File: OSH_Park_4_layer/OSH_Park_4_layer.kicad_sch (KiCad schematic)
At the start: 2 parts

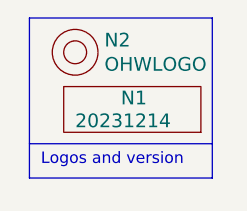
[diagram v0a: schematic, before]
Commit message: updated to kicad V8
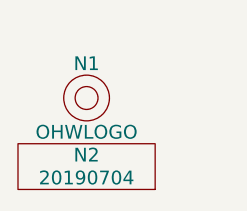
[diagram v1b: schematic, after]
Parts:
- removed N1: 20231214, SquantorLabels:Label_Generic, symbol SquantorLabels:VYYYYMMDD
- removed N2: OHWLOGO, Symbol:OSHW-Symbol_6.7x6mm_SilkScreen, symbol SquantorLabels:OHWLOGO
- added N1: OHWLOGO, Symbols:OSHW-Symbol_6.7x6mm_SilkScreen, symbol SquantorLabels:OHWLOGO
- added N2: 20190704, SquantorLabels:Label_version, symbol SquantorLabels:VYYYYMMDD
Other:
- note removed: "Logos and version"
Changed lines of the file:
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@@
 	(generator_version "8.0")
 	(paper "A4")
-	(polyline
-		(pts
-			(xy 15.24 177.8) (xy 15.24 195.58)
-		)
-		(stroke
-			(width 0)
-			(type default)
-		)
-	)
-	(polyline
-		(pts
-			(xy 35.56 177.8) (xy 15.24 177.8)
-		)
-		(stroke
-			(width 0)
-			(type default)
-		)
-	)
-	(polyline
-		(pts
-			(xy 35.56 195.58) (xy 35.56 177.8)
-		)
-		(stroke
-			(width 0)
-			(type default)
-		)
-	)
-	(polyline
-		(pts
-			(xy 15.24 195.58) (xy 35.56 195.58)
-		)
-		(stroke
-			(width 0)
-			(type default)
-		)
-	)
-	(polyline
-		(pts
-			(xy 15.24 191.77) (xy 35.56 191.77)
-		)
-		(stroke
-			(width 0)
-			(type default)
-		)
-	)
-	(text "Logos and version"
-		(exclude_from_sim no)
-		(at 16.51 194.31 0)
-		(effects
-			(font
-				(size 1.27 1.27)
-			)
-			(justify left bottom)
-		)
-	)
 	(symbol
 		(lib_id "SquantorLabels:VYYYYMMDD")
-		(at 26.67 189.23 0)
+		(at 21.59 195.58 0)
 		(unit 1)
 		(exclude_from_sim no)
@@
 		(on_board yes)
 		(dnp no)
-		(property "Reference" "N1"
-			(at 25.4 186.69 0)
+		(property "Reference" "N2"
+			(at 21.59 193.04 0)
 			(effects
 				(font
 					(size 1.524 1.524)
 				)
-				(justify left)
 			)
 		)
-		(property "Value" "20231214"
-			(at 20.32 189.23 0)
+		(property "Value" "20190704"
+			(at 21.59 195.58 0)
 			(effects
 				(font
 					(size 1.524 1.524)
 				)
-				(justify left)
 			)
 		)
-		(property "Footprint" "SquantorLabels:Label_Generic"
-			(at 26.67 189.23 0)
+		(property "Footprint" "SquantorLabels:Label_version"
+			(at 21.59 195.58 0)
 			(effects
 				(font
@@
 		)
 		(property "Datasheet" ""
-			(at 26.67 189.23 0)
+			(at 21.59 195.58 0)
 			(effects
 				(font
@@
 		)
 		(property "Description" ""
-			(at 26.67 189.23 0)
+			(at 21.59 195.58 0)
 			(effects
 				(font
@@
 		)
 		(instances
-			(project "Aisler_simple_2_layer"
-				(path "/646d9e91-59b4-4865-a2fc-29780ed32563"
-					(reference "N1")
+			(project ""
+				(path "/136ceeb2-ade5-451e-9d73-32125e93dd8b"
+					(reference "N2")
 					(unit 1)
 				)
@@
 	(symbol
 		(lib_id "SquantorLabels:OHWLOGO")
-		(at 20.32 181.61 0)
+		(at 21.59 186.69 0)
 		(unit 1)
 		(exclude_from_sim no)
@@
 		(on_board yes)
 		(dnp no)
-		(property "Reference" "N2"
-			(at 23.5712 180.2638 0)
+		(property "Reference" "N1"
+			(at 21.59 182.88 0)
 			(effects
 				(font
 					(size 1.524 1.524)
 				)
-				(justify left)
 			)
 		)
 		(property "Value" "OHWLOGO"
-			(at 23.5712 182.9562 0)
+			(at 21.59 190.5 0)
 			(effects
 				(font
 					(size 1.524 1.524)
 				)
-				(justify left)
 			)
 		)
-		(property "Footprint" "Symbol:OSHW-Symbol_6.7x6mm_SilkScreen"
-			(at 20.32 181.61 0)
+		(property "Footprint" "Symbols:OSHW-Symbol_6.7x6mm_SilkScreen"
+			(at 21.59 186.69 0)
 			(effects
 				(font
@@
 		)
 		(property "Datasheet" ""
-			(at 20.32 181.61 0)
+			(at 21.59 186.69 0)
 			(effects
 				(font
@@
 		)
 		(property "Description" ""
-			(at 20.32 181.61 0)
+			(at 21.59 186.69 0)
 			(effects
 				(font
@@
 		)
 		(instances
-			(project "Aisler_simple_2_layer"
-				(path "/646d9e91-59b4-4865-a2fc-29780ed32563"
-					(reference "N2")
+			(project ""
+				(path "/136ceeb2-ade5-451e-9d73-32125e93dd8b"
+					(reference "N1")
 					(unit 1)
 				)
